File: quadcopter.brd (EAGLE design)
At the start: 127.2 x 127.2 mm, 77 parts, among them J1 AVR_SPI_PRG_6NS, J3 HEADER-0.1IN-2POS-FEMALE, J4 HEADER-0.1IN-2POS-FEMALE, J5 HEADER-0.1IN-2POS-FEMALE, J6 HEADER-0.1IN-2POS-FEMALE, J8 HEADER-0.1IN-2POS-FEMALE, SW1 PUSHBUTTON_SMD-VERTICAL, SW2 PUSHBUTTON_SMD-VERTICAL, U1 ATMEGA128RFA1

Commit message: made farady cage tighter, added heat sink
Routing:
- net GND: track 251.7 -> 245.4 mm, vias 7 -> 22
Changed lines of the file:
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@@
 <setting verticaltext="up"/>
 </settings>
-<grid distance="1" unitdist="mil" unit="mil" style="lines" multiple="1" display="yes" altdistance="0.025" altunitdist="inch" altunit="inch"/>
+<grid distance="0.5" unitdist="mm" unit="mm" style="lines" multiple="1" display="yes" altdistance="0.025" altunitdist="inch" altunit="inch"/>
 <layers>
 <layer number="1" name="Top" color="4" fill="1" visible="yes" active="yes"/>
@@
 <layer number="17" name="Pads" color="2" fill="1" visible="yes" active="yes"/>
 <layer number="18" name="Vias" color="2" fill="1" visible="yes" active="yes"/>
-<layer number="19" name="Unrouted" color="6" fill="1" visible="yes" active="yes"/>
+<layer number="19" name="Unrouted" color="6" fill="1" visible="no" active="yes"/>
 <layer number="20" name="Dimension" color="15" fill="1" visible="yes" active="yes"/>
-<layer number="21" name="tPlace" color="7" fill="1" visible="yes" active="yes"/>
+<layer number="21" name="tPlace" color="7" fill="1" visible="no" active="yes"/>
 <layer number="22" name="bPlace" color="7" fill="1" visible="yes" active="yes"/>
 <layer number="23" name="tOrigins" color="15" fill="1" visible="yes" active="yes"/>
@@
 <layer number="38" name="bTest" color="7" fill="1" visible="yes" active="yes"/>
 <layer number="39" name="tKeepout" color="4" fill="11" visible="yes" active="yes"/>
-<layer number="40" name="bKeepout" color="1" fill="11" visible="no" active="yes"/>
-<layer number="41" name="tRestrict" color="4" fill="10" visible="no" active="yes"/>
-<layer number="42" name="bRestrict" color="1" fill="10" visible="no" active="yes"/>
+<layer number="40" name="bKeepout" color="1" fill="11" visible="yes" active="yes"/>
+<layer number="41" name="tRestrict" color="4" fill="10" visible="yes" active="yes"/>
+<layer number="42" name="bRestrict" color="1" fill="10" visible="yes" active="yes"/>
 <layer number="43" name="vRestrict" color="2" fill="10" visible="yes" active="yes"/>
 <layer number="44" name="Drills" color="7" fill="1" visible="yes" active="yes"/>
@@
 <vertex x="-4.572" y="9.525"/>
 <vertex x="-4.699" y="9.525"/>
-</polygon>
-<polygon width="0.762" layer="41">
-<vertex x="-4.826" y="18.542"/>
-<vertex x="4.318" y="18.542"/>
-<vertex x="4.318" y="9.525"/>
-<vertex x="-4.445" y="9.525"/>
-<vertex x="-4.445" y="9.779"/>
-<vertex x="-4.826" y="9.779"/>
 </polygon>
 </plain>
@@
 <wire x1="-0.75" y1="18.881" x2="-1.25" y2="18.881" width="0.2032" layer="1"/>
 <wire x1="-0.762" y1="18.869" x2="-0.75" y2="18.881" width="0.2032" layer="1"/>
-<via x="2.722" y="20.96" extent="1-16" drill="0.6"/>
+<via x="2.5" y="21" extent="1-16" drill="0.6"/>
 <wire x1="-4.318" y1="21.463" x2="-4.26" y2="21.5" width="0.254" layer="1"/>
 <wire x1="-1.27" y1="18.923" x2="-1.25" y2="18.881" width="0.254" layer="1"/>
@@
 <wire x1="-4.881" y1="16.256" x2="-4.881" y2="16.25" width="0.2032" layer="1"/>
 <wire x1="-2.7432" y1="16.256" x2="-4.881" y2="16.256" width="0.2032" layer="1"/>
-<wire x1="-2.7432" y1="16.256" x2="-2.7432" y2="17.7292" width="0.2032" layer="1"/>
 <wire x1="-2.7432" y1="17.7292" x2="-1.25" y2="17.7292" width="0.2032" layer="1"/>
 <wire x1="-2.75" y1="9.119" x2="-2.7432" y2="9.119" width="0.2032" layer="1"/>
 <wire x1="-3.7592" y1="9.119" x2="-3.75" y2="9.119" width="0.2032" layer="1"/>
-<wire x1="2.2606" y1="10.287" x2="-2.7432" y2="10.287" width="0.2032" layer="1"/>
+<wire x1="2.2606" y1="10.287" x2="-2.5" y2="10.287" width="0.2032" layer="1"/>
+<wire x1="-2.5" y1="10.287" x2="-2.7432" y2="10.287" width="0.2032" layer="1"/>
 <wire x1="2.2606" y1="10.287" x2="2.2606" y2="9.119" width="0.2032" layer="1"/>
 <wire x1="2.2606" y1="9.119" x2="2.25" y2="9.119" width="0.2032" layer="1"/>
@@
 <wire x1="-2.7432" y1="10.287" x2="-2.7432" y2="9.1258" width="0.2032" layer="1"/>
 <wire x1="-2.7432" y1="9.1258" x2="-2.75" y2="9.119" width="0.2032" layer="1"/>
-<wire x1="-2.7432" y1="10.287" x2="-2.7432" y2="16.256" width="0.2032" layer="1"/>
 <wire x1="-5" y1="-6.395" x2="-5" y2="-6.3814" width="0.2032" layer="1"/>
 <wire x1="-5" y1="-6.3814" x2="-3.0028" y2="-6.3814" width="0.762" layer="1"/>
@@
 <wire x1="30" y1="-2.7" x2="28.636" y2="-4.064" width="0.2032" layer="1"/>
 <wire x1="28.636" y1="-4.064" x2="17.9832" y2="-4.064" width="0.2032" layer="1"/>
-<via x="2.667" y="25.019" extent="1-16" drill="0.381"/>
-<via x="2.698" y="22.873" extent="1-16" drill="0.381"/>
+<via x="3" y="26" extent="1-16" drill="0.381"/>
+<via x="2.5" y="23" extent="1-16" drill="0.381"/>
 <wire x1="19.436" y1="23.5" x2="12.3698" y2="23.5" width="0.762" layer="1"/>
 <wire x1="12.3698" y1="23.5" x2="12.3698" y2="18.5674" width="0.762" layer="1"/>
@@
 <wire x1="-26" y1="-5.857" x2="-30" y2="-5.857" width="0.762" layer="1"/>
 <wire x1="-26" y1="-12" x2="-26" y2="-11" width="0.762" layer="1"/>
+<via x="-3" y="26" extent="1-16" drill="0.381"/>
+<via x="-6.5" y="24" extent="1-16" drill="0.381"/>
+<via x="-6.5" y="22" extent="1-16" drill="0.381"/>
+<via x="5" y="26" extent="1-16" drill="0.381"/>
+<via x="-5" y="26" extent="1-16" drill="0.381"/>
+<via x="5" y="24" extent="1-16" drill="0.381"/>
+<polygon width="0.4064" layer="1">
+<vertex x="-3.75" y="17.75"/>
+<vertex x="3.75" y="17.75"/>
+<vertex x="3.75" y="10.25"/>
+<vertex x="-3.75" y="10.25"/>
+</polygon>
+<via x="-2.5" y="16.5" extent="1-16" drill="0.381"/>
+<via x="0" y="16.5" extent="1-16" drill="0.381"/>
+<via x="2.5" y="16.5" extent="1-16" drill="0.381"/>
+<via x="2.5" y="14" extent="1-16" drill="0.381"/>
+<via x="2.5" y="11.5" extent="1-16" drill="0.381"/>
+<via x="0" y="11.5" extent="1-16" drill="0.381"/>
+<via x="-2.5" y="11.5" extent="1-16" drill="0.381"/>
+<via x="-2.5" y="14" extent="1-16" drill="0.381"/>
+<via x="0" y="14" extent="1-16" drill="0.381"/>
+<wire x1="-2.5" y1="11.5" x2="-2.5" y2="10.287" width="0.4064" layer="1"/>
 </signal>
 <signal name="RFP">
@@
 <wire x1="29.8704" y1="14.6685" x2="29.955" y2="14.662" width="0.2032" layer="1"/>
 <wire x1="-20.3581" y1="13.7795" x2="-20.447" y2="13.7795" width="0.2032" layer="16"/>
-<wire x1="-6.6675" y1="19.8247" x2="-6.6675" y2="19.9136" width="0.2032" layer="1"/>
+<wire x1="-6.5" y1="20" x2="-6.6675" y2="19.9136" width="0.2032" layer="1"/>
 <wire x1="-6.6675" y1="15.7353" x2="-6.6675" y2="19.3675" width="0.2032" layer="16"/>
-<wire x1="-6.6675" y1="19.3675" x2="-6.6675" y2="19.8247" width="0.2032" layer="16"/>
+<wire x1="-6.6675" y1="19.3675" x2="-6.5" y2="20" width="0.2032" layer="16"/>
 <wire x1="-6.6675" y1="19.9136" x2="-6.604" y2="19.971" width="0.2032" layer="1"/>
 <via x="-20.447" y="13.7795" extent="1-16" drill="0.381"/>
 <via x="27.686" y="14.6685" extent="1-16" drill="0.381"/>
-<via x="-6.6675" y="19.8247" extent="1-16" drill="0.381"/>
+<via x="-6.5" y="20" extent="1-16" drill="0.381"/>
 <wire x1="23.01875" y1="19.3675" x2="27.6225" y2="14.76375" width="0.1524" layer="16"/>
 <wire x1="-6.6675" y1="19.3675" x2="23.01875" y2="19.3675" width="0.1524" layer="16"/>

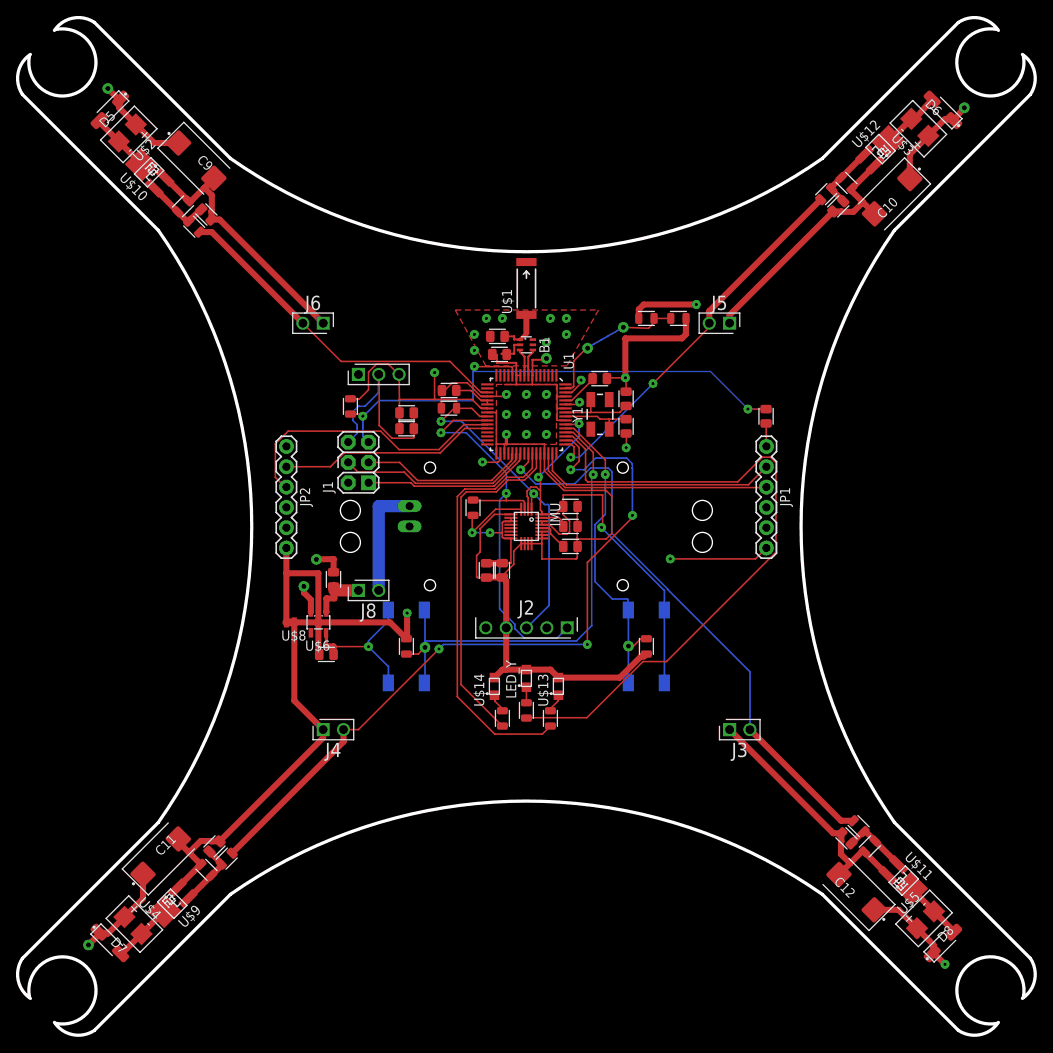
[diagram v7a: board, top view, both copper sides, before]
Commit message: More gnd cleaning
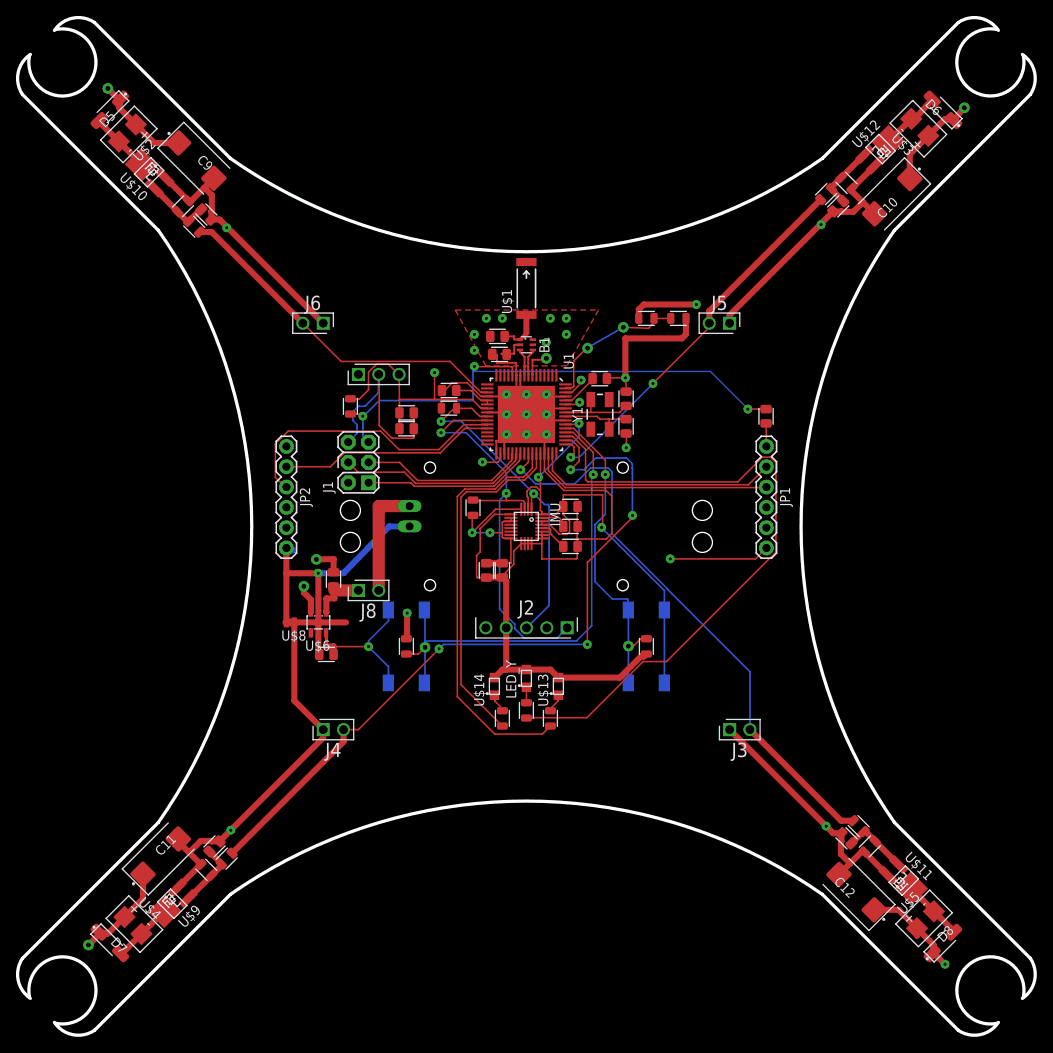
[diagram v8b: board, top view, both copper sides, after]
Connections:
- net GND: now also U1.65
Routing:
- net GND: track 245.4 -> 266.3 mm, vias 22 -> 23
- net BAT_GND: vias 1 -> 5
